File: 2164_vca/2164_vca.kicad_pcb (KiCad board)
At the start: 2 copper layers, 268.6 x 131.9 mm, 80 parts, among them J1 Power Connector, J10 Conn_01x03_Pin, J11 CV B, J12 To J3, J13 Conn_01x03_Pin, J14 To J3, J15 Conn_01x03_Pin, J16 In B, J17 Out B, J18 To J3, J19 Conn_01x03_Pin, J2 CV A, J3 To J3, J4 Conn_01x03_Pin, J5 To J3, J6 Conn_01x03_Pin, J7 In A, J8 Out A, J9 To J3, U1 SSI2164, U2 TL074

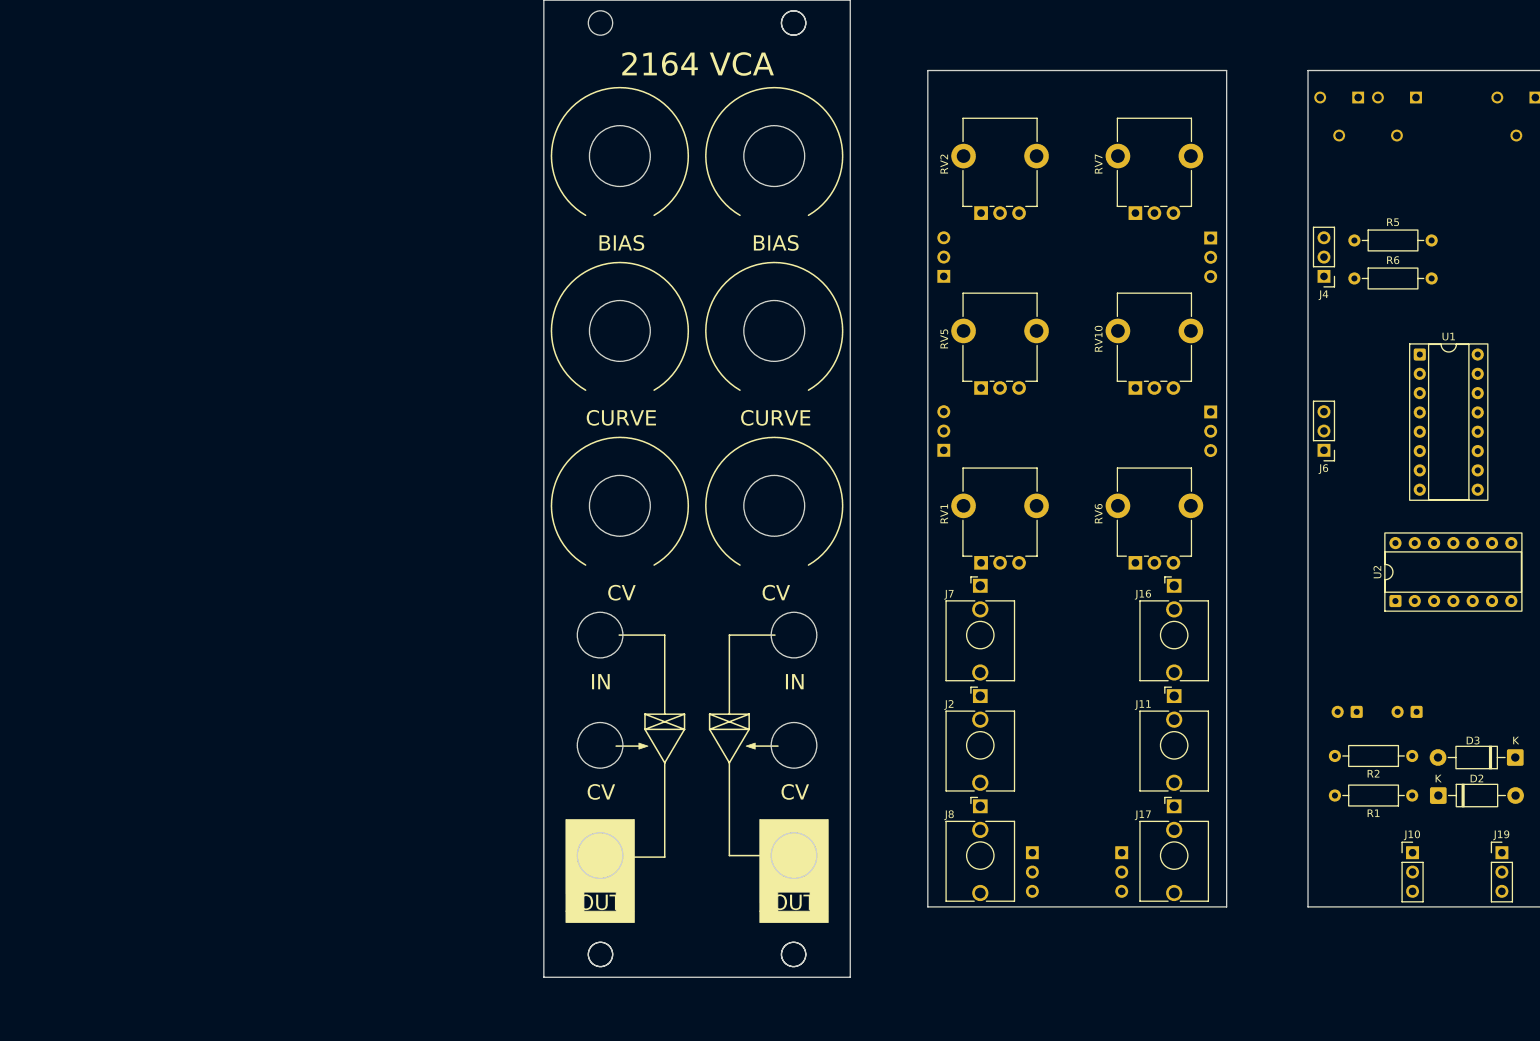
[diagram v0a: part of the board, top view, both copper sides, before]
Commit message: 2164 vca: redesign front panel
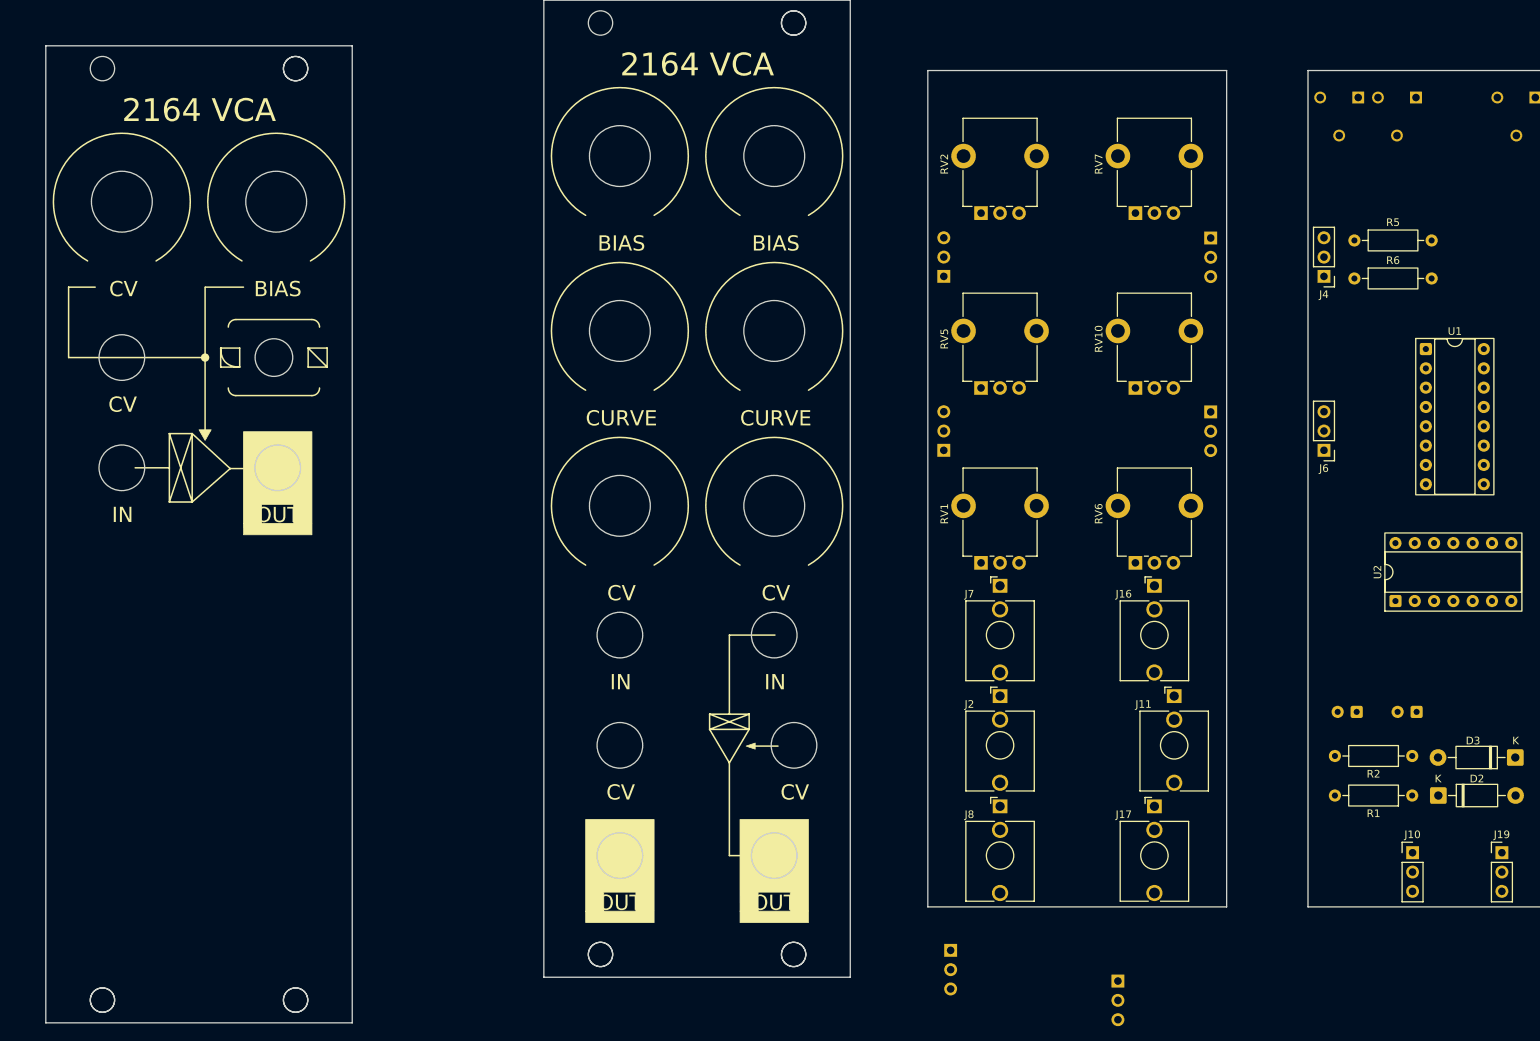
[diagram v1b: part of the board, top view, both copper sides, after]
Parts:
- added ?: , , F.Cu at (-38.0, 151.5)
- added ?: , , F.Cu at (-12.7, 151.5)
- added ?: , , F.Cu at (-12.7, 29.0)
- added REF**: MountingHole_3.2mm_M3, MountingHole:MountingHole_3.2mm_M3, F.Cu at (-38.0, 151.5)
- added REF**: MountingHole_3.2mm_M3, MountingHole:MountingHole_3.2mm_M3, F.Cu at (-12.7, 29.0)
- added REF**: MountingHole_3.2mm_M3, MountingHole:MountingHole_3.2mm_M3, F.Cu at (-38.0, 29.0)
- added REF**: MountingHole_3.2mm_M3, MountingHole:MountingHole_3.2mm_M3, F.Cu at (-12.7, 151.5)
- moved J18 16.9 mm to (95.5, 149.0)
- moved J9 16.7 mm to (73.5, 145.0)
- moved J16 2.60 mm to (100.3, 97.0)
- moved J17 2.60 mm to (100.3, 126.0)
- moved J2 2.60 mm to (80.0, 111.5)
- moved J7 2.60 mm to (80.0, 97.0)
- moved J8 2.60 mm to (80.0, 126.0)
- moved U1 1.08 mm to (136.0, 65.9)
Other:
- board size 268.6 x 131.9 mm -> 268.6 x 134.5 mm
